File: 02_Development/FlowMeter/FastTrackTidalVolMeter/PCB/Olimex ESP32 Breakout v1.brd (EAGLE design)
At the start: 45 x 30 mm, 5 parts, among them CN1 1X4-BIG

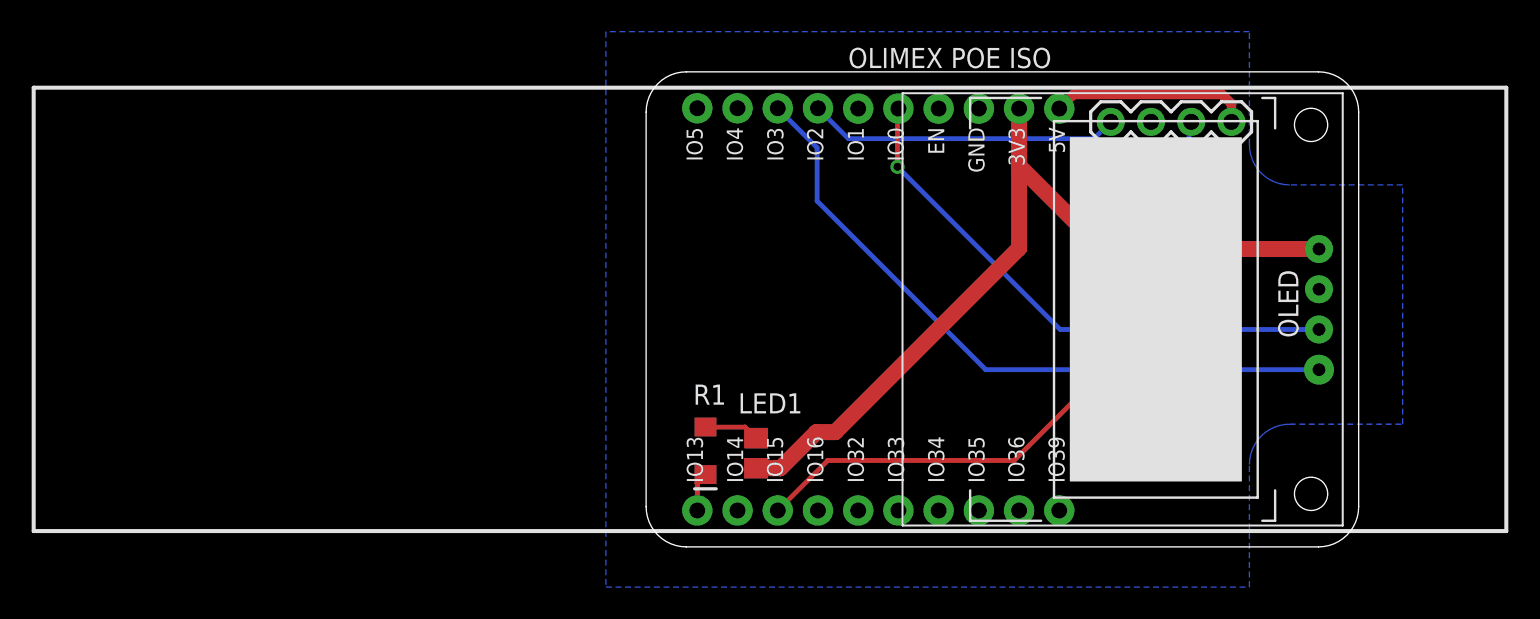
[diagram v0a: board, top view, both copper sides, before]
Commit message: Adjustments for mechanical fit
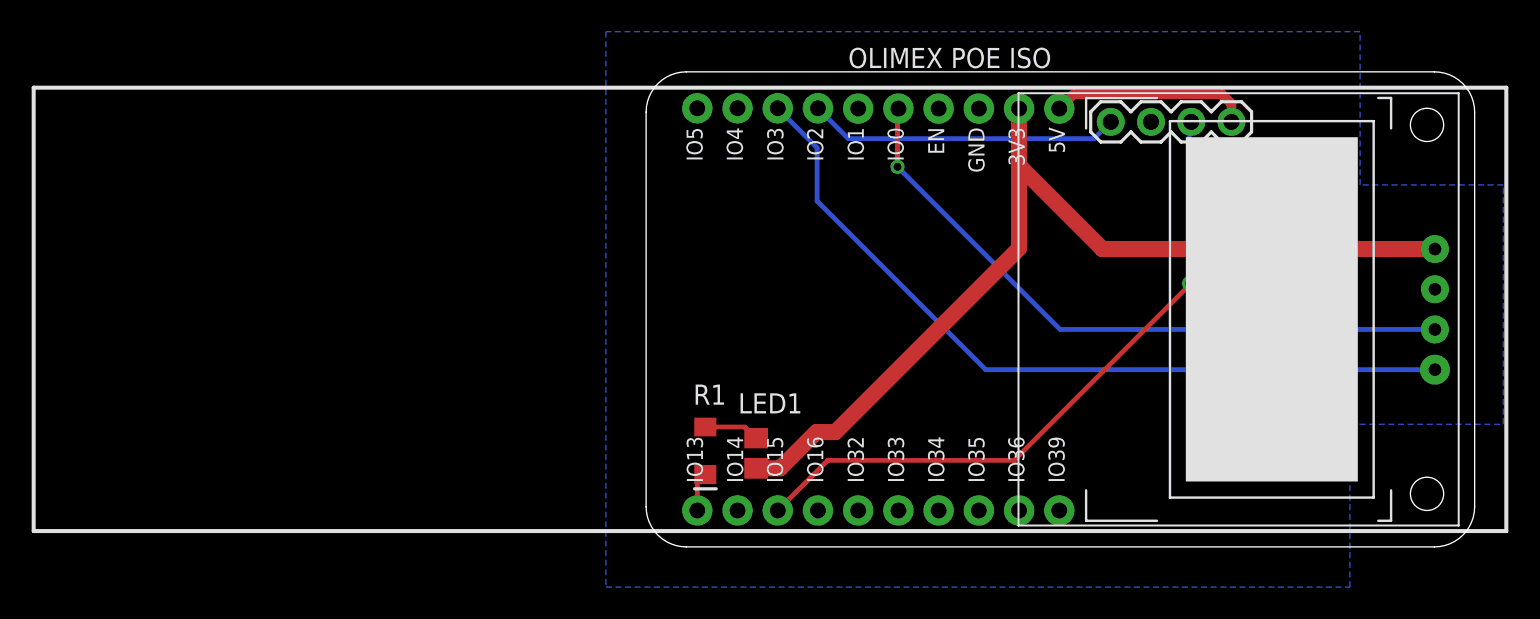
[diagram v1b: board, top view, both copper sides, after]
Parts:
- moved U$3 7.32 mm to (51.3, 15.0)
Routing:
- net GPIO0-SCL(OLED): track 34.6 -> 41.9 mm
- net 3V3: track 52.3 -> 59.6 mm
- net GPIO3-SDA(OLED): track 43.0 -> 50.3 mm
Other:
- board size 45 x 30 mm -> 52.3 x 30 mm
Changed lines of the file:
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@@
 <grid distance="25" unitdist="mil" unit="mil" style="lines" multiple="1" display="no" altdistance="5" altunitdist="mil" altunit="mil"/>
 <layers>
-<layer number="1" name="Top" color="4" fill="1" visible="no" active="yes"/>
+<layer number="1" name="Top" color="4" fill="1" visible="yes" active="yes"/>
 <layer number="2" name="Route2" color="16" fill="1" visible="no" active="no"/>
 <layer number="3" name="Route3" color="17" fill="1" visible="no" active="no"/>
@@
 <layer number="17" name="Pads" color="2" fill="1" visible="yes" active="yes"/>
 <layer number="18" name="Vias" color="2" fill="1" visible="yes" active="yes"/>
-<layer number="19" name="Unrouted" color="6" fill="1" visible="no" active="yes"/>
+<layer number="19" name="Unrouted" color="6" fill="1" visible="yes" active="yes"/>
 <layer number="20" name="Dimension" color="24" fill="1" visible="yes" active="yes"/>
-<layer number="21" name="tPlace" color="7" fill="1" visible="no" active="yes"/>
-<layer number="22" name="bPlace" color="7" fill="1" visible="yes" active="yes"/>
-<layer number="23" name="tOrigins" color="15" fill="1" visible="no" active="yes"/>
+<layer number="21" name="tPlace" color="7" fill="1" visible="yes" active="yes"/>
+<layer number="22" name="bPlace" color="7" fill="1" visible="no" active="yes"/>
+<layer number="23" name="tOrigins" color="15" fill="1" visible="yes" active="yes"/>
 <layer number="24" name="bOrigins" color="15" fill="1" visible="no" active="yes"/>
-<layer number="25" name="tNames" color="7" fill="1" visible="no" active="yes"/>
-<layer number="26" name="bNames" color="7" fill="1" visible="yes" active="yes"/>
+<layer number="25" name="tNames" color="7" fill="1" visible="yes" active="yes"/>
+<layer number="26" name="bNames" color="7" fill="1" visible="no" active="yes"/>
 <layer number="27" name="tValues" color="7" fill="1" visible="no" active="yes"/>
 <layer number="28" name="bValues" color="7" fill="1" visible="no" active="yes"/>
 <layer number="29" name="tStop" color="7" fill="3" visible="no" active="yes"/>
-<layer number="30" name="bStop" color="7" fill="6" visible="yes" active="yes"/>
+<layer number="30" name="bStop" color="7" fill="6" visible="no" active="yes"/>
 <layer number="31" name="tCream" color="7" fill="4" visible="no" active="yes"/>
 <layer number="32" name="bCream" color="7" fill="5" visible="no" active="yes"/>
@@
 <layer number="37" name="tTest" color="7" fill="1" visible="no" active="yes"/>
 <layer number="38" name="bTest" color="7" fill="1" visible="no" active="yes"/>
-<layer number="39" name="tKeepout" color="4" fill="11" visible="no" active="yes"/>
+<layer number="39" name="tKeepout" color="4" fill="11" visible="yes" active="yes"/>
 <layer number="40" name="bKeepout" color="1" fill="11" visible="no" active="yes"/>
-<layer number="41" name="tRestrict" color="4" fill="10" visible="no" active="yes"/>
+<layer number="41" name="tRestrict" color="4" fill="10" visible="yes" active="yes"/>
 <layer number="42" name="bRestrict" color="1" fill="10" visible="no" active="yes"/>
 <layer number="43" name="vRestrict" color="2" fill="10" visible="no" active="yes"/>
@@
 <layer number="49" name="Reference" color="7" fill="1" visible="no" active="yes"/>
 <layer number="50" name="dxf" color="7" fill="1" visible="no" active="no"/>
-<layer number="51" name="tDocu" color="7" fill="1" visible="no" active="yes"/>
+<layer number="51" name="tDocu" color="7" fill="1" visible="yes" active="yes"/>
 <layer number="52" name="bDocu" color="7" fill="1" visible="no" active="yes"/>
 <layer number="53" name="tGND_GNDA" color="7" fill="9" visible="no" active="no"/>
@@
 </layers>
 <board>
+<fusionsync huburn="a.YnVzaW5lc3M6ZmFjdG9yeW9wdGlj" projecturn="a.YnVzaW5lc3M6ZmFjdG9yeW9wdGljIzIwMjEwODI1NDM3NTg0OTMx" f3durn="urn:adsk.wipprod:dm.lineage:du4sK8XgQCusDuCg-pj6mg" pcbguid="7ce49bbb-af08-4c74-95dd-39b1005455e2" lastpulledtime="" lastsyncedchangeguid="" latestrevisionid="de7603bb-de8d-4b99-95bd-b855d0dd0d57" lastsyncedrevisionid="de7603bb-de8d-4b99-95bd-b855d0dd0d57" lastboardhashguid="b1065ac0-79e1-826b-3e0f-b07ffe149d0b" lastpushedtime="2021-09-07T00:42:18Z" linktopcb3d="true"/>
 <plain>
-<wire x1="2.54" y1="0" x2="42.46" y2="0" width="0" layer="20"/>
-<wire x1="42.46" y1="0" x2="45" y2="2.54" width="0" layer="20" curve="90"/>
-<wire x1="45" y1="2.54" x2="45" y2="27.46" width="0" layer="20"/>
-<wire x1="45" y1="27.46" x2="42.46" y2="30" width="0" layer="20" curve="90"/>
-<wire x1="42.46" y1="30" x2="2.54" y2="30" width="0" layer="20"/>
+<wire x1="2.54" y1="0" x2="49.783" y2="0" width="0" layer="20"/>
+<wire x1="49.783" y1="0" x2="52.323" y2="2.54" width="0" layer="20" curve="90"/>
+<wire x1="52.323" y1="2.54" x2="52.323" y2="27.46" width="0" layer="20"/>
+<wire x1="52.323" y1="27.46" x2="49.783" y2="30" width="0" layer="20" curve="90"/>
+<wire x1="49.783" y1="30" x2="2.54" y2="30" width="0" layer="20"/>
 <wire x1="2.54" y1="30" x2="0" y2="27.46" width="0" layer="20" curve="90"/>
 <wire x1="0" y1="27.46" x2="0" y2="2.54" width="0" layer="20"/>
@@
 <text x="31.115" y="21.59" size="1.27" layer="26" font="vector" ratio="14" rot="MR90">GND</text>
 <text x="28.575" y="21.59" size="1.27" layer="26" font="vector" ratio="14" rot="MR90">SDA</text>
-<text x="40.64" y="18.415" size="1.27" layer="26" font="vector" ratio="14" rot="MR0">+3.3V</text>
-<text x="40.64" y="13.335" size="1.27" layer="26" font="vector" ratio="14" rot="MR0">SCL</text>
-<text x="40.64" y="10.795" size="1.27" layer="26" font="vector" ratio="14" rot="MR0">SDA</text>
-<text x="40.64" y="15.875" size="1.27" layer="26" font="vector" ratio="14" rot="MR0">GND</text>
+<text x="48.26" y="18.415" size="1.27" layer="26" font="vector" ratio="14" rot="MR0">+3.3V</text>
+<text x="48.26" y="13.335" size="1.27" layer="26" font="vector" ratio="14" rot="MR0">SCL</text>
+<text x="48.26" y="10.795" size="1.27" layer="26" font="vector" ratio="14" rot="MR0">SDA</text>
+<text x="48.26" y="15.875" size="1.27" layer="26" font="vector" ratio="14" rot="MR0">GND</text>
 </plain>
 <attributes>
@@
 <attribute name="VALUE" x="4.408" y="8.455" size="1.27" layer="27" font="vector" ratio="13" rot="R270"/>
 </element>
-<element name="U$3" library="oled" package=".96&quot;OLED-TOPHOLESONLY" value=".91&quot;OLEDTOPHOLESONLY" x="43.9928" y="15" smashed="yes" rot="R270"/>
+<element name="U$3" library="oled" package=".96&quot;OLED-TOPHOLESONLY" value=".91&quot;OLEDTOPHOLESONLY" x="51.3158" y="15" smashed="yes" rot="R270"/>
 <element name="CN1" library="adafruit" library_urn="urn:adsk.eagle:library:420" package="1X04-BIG" package3d_urn="urn:adsk.eagle:package:6240658/1" value="1X4-BIG" x="36.965" y="26.841" smashed="yes" rot="R180">
 <attribute name="NAME" x="38.4878" y="24.9762" size="1.27" layer="26" font="vector" ratio="14" rot="MR90"/>
@@
 <vertex x="-2.54" y="32.5374"/>
 <vertex x="-2.54" y="-2.54"/>
-<vertex x="38.1" y="-2.54"/>
-<vertex x="38.1" y="5.207" curve="-90"/>
-<vertex x="40.64" y="7.747"/>
-<vertex x="47.7774" y="7.747"/>
-<vertex x="47.7774" y="22.86"/>
-<vertex x="40.64" y="22.86" curve="-90"/>
-<vertex x="38.1" y="25.4"/>
-<vertex x="38.1" y="32.5374"/>
+<vertex x="44.45" y="-2.54"/>
+<vertex x="44.45" y="7.747"/>
+<vertex x="54.1274" y="7.747"/>
+<vertex x="54.1274" y="22.86"/>
+<vertex x="45.085" y="22.86"/>
+<vertex x="45.085" y="32.5374"/>
 </polygon>
 <contactref element="U$3" pad="GND"/>
@@
 <contactref element="U$1" pad="2"/>
 <wire x1="23.5525" y1="27.68" x2="23.5525" y2="24.0725" width="1.016" layer="1"/>
-<wire x1="28.815" y1="18.81" x2="42.4928" y2="18.81" width="1.016" layer="1"/>
+<wire x1="28.815" y1="18.81" x2="49.8158" y2="18.81" width="1.016" layer="1"/>
 <wire x1="23.5525" y1="24.0725" x2="28.815" y2="18.81" width="1.016" layer="1"/>
 <wire x1="23.5525" y1="24.0725" x2="23.5525" y2="18.8535" width="1.016" layer="1"/>
@@
 <contactref element="U$3" pad="SCL"/>
 <contactref element="U$1" pad="5"/>
-<wire x1="42.4928" y1="13.73" x2="26.148" y2="13.73" width="0.3048" layer="16"/>
+<wire x1="49.8158" y1="13.73" x2="26.148" y2="13.73" width="0.3048" layer="16"/>
 <wire x1="26.148" y1="13.73" x2="15.875" y2="24.003" width="0.3048" layer="16"/>
 <via x="15.875" y="24.003" extent="1-16" drill="0.5"/>
@@
 <wire x1="10.795" y1="25.2175" x2="10.795" y2="21.844" width="0.3048" layer="16"/>
 <wire x1="10.795" y1="21.844" x2="21.449" y2="11.19" width="0.3048" layer="16"/>
-<wire x1="21.449" y1="11.19" x2="42.4928" y2="11.19" width="0.3048" layer="16"/>
+<wire x1="21.449" y1="11.19" x2="49.8158" y2="11.19" width="0.3048" layer="16"/>
 </signal>
 <signal name="GPIO15-SCL(SENSIRION)">
@@
 </note>
 <note version="8.3" severity="warning">
+Since Version 8.3, EAGLE supports Fusion synchronisation.
+This feature will not be available in this version and saving
+the document will break the link to the Fusion PCB feature.
+</note>
+<note version="8.3" severity="warning">
